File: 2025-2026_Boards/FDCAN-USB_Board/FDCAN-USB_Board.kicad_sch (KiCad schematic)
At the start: 0 parts

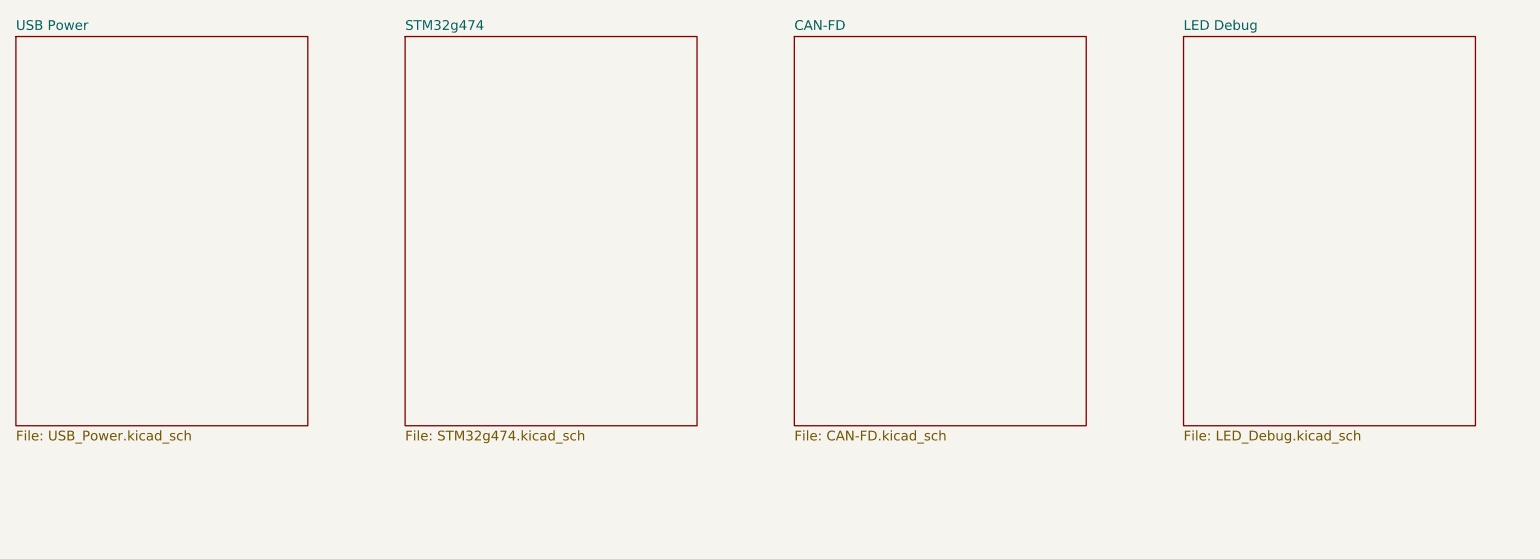
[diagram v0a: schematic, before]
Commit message: Schematic done
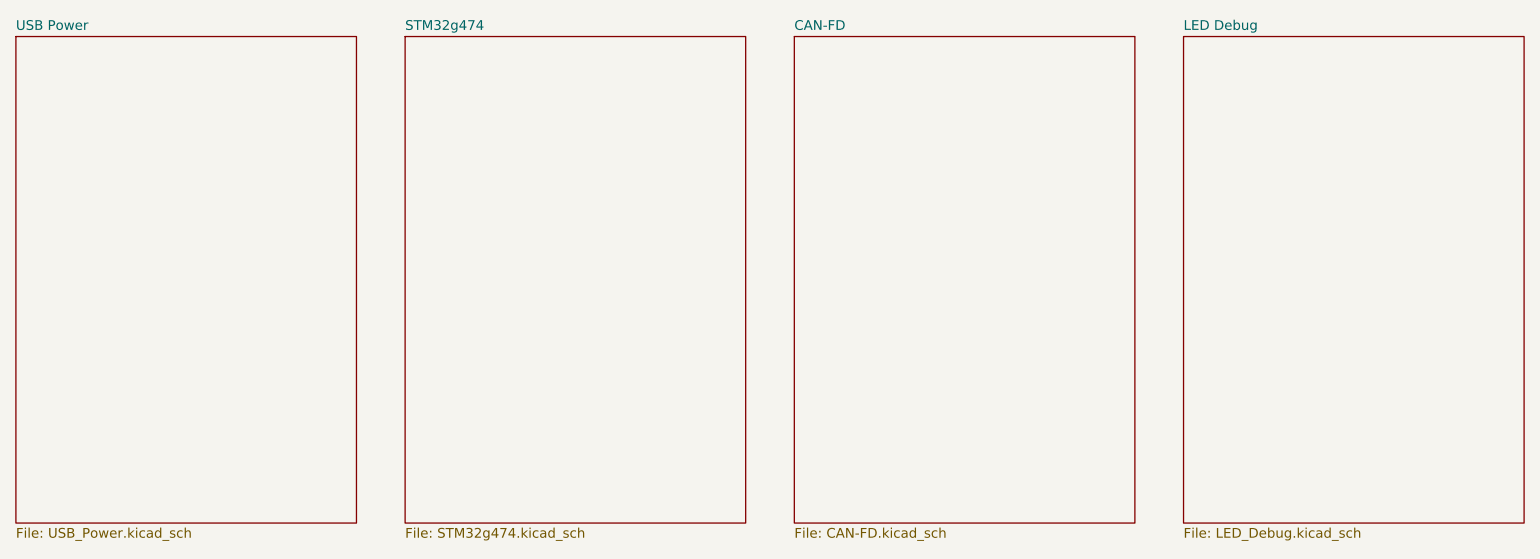
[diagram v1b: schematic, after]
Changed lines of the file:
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@@
 	(sheet
 		(at 88.9 38.1)
-		(size 38.1 50.8)
+		(size 44.45 63.5)
 		(exclude_from_sim no)
 		(in_bom yes)
@@
 		)
 		(property "Sheetfile" "STM32g474.kicad_sch"
-			(at 88.9 89.4846 0)
+			(at 88.9 102.1846 0)
 			(effects
 				(font
@@
 	(sheet
 		(at 38.1 38.1)
-		(size 38.1 50.8)
+		(size 44.45 63.5)
 		(exclude_from_sim no)
 		(in_bom yes)
@@
 		)
 		(property "Sheetfile" "USB_Power.kicad_sch"
-			(at 38.1 89.4846 0)
+			(at 38.1 102.1846 0)
 			(effects
 				(font
@@
 	(sheet
 		(at 139.7 38.1)
-		(size 38.1 50.8)
+		(size 44.45 63.5)
 		(exclude_from_sim no)
 		(in_bom yes)
@@
 		)
 		(property "Sheetfile" "CAN-FD.kicad_sch"
-			(at 139.7 89.4846 0)
+			(at 139.7 102.1846 0)
 			(effects
 				(font
@@
 	(sheet
 		(at 190.5 38.1)
-		(size 38.1 50.8)
+		(size 44.45 63.5)
 		(exclude_from_sim no)
 		(in_bom yes)
@@
 		)
 		(property "Sheetfile" "LED_Debug.kicad_sch"
-			(at 190.5 89.4846 0)
+			(at 190.5 102.1846 0)
 			(effects
 				(font
